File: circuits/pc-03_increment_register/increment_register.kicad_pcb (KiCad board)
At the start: 2 copper layers, 99.1 x 99.1 mm, 25 parts, among them J1 Conn_01x10, U1 74HC273, U10 4081, U11 4070, U12 4070, U13 4011, U2 74HC273, U3 74HC244, U4 74HC244, U5 74LS283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

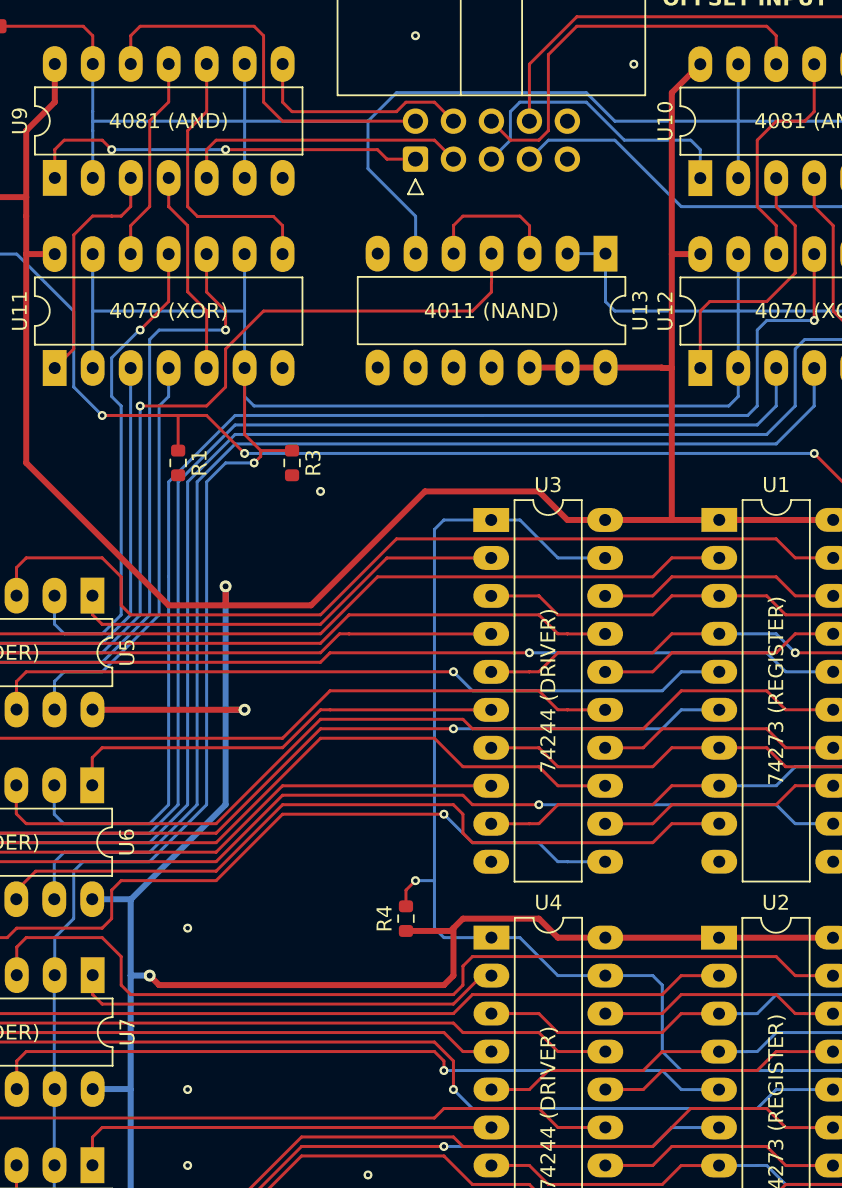
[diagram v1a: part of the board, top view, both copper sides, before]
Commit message: add filter and decoupling capacitors to all boards
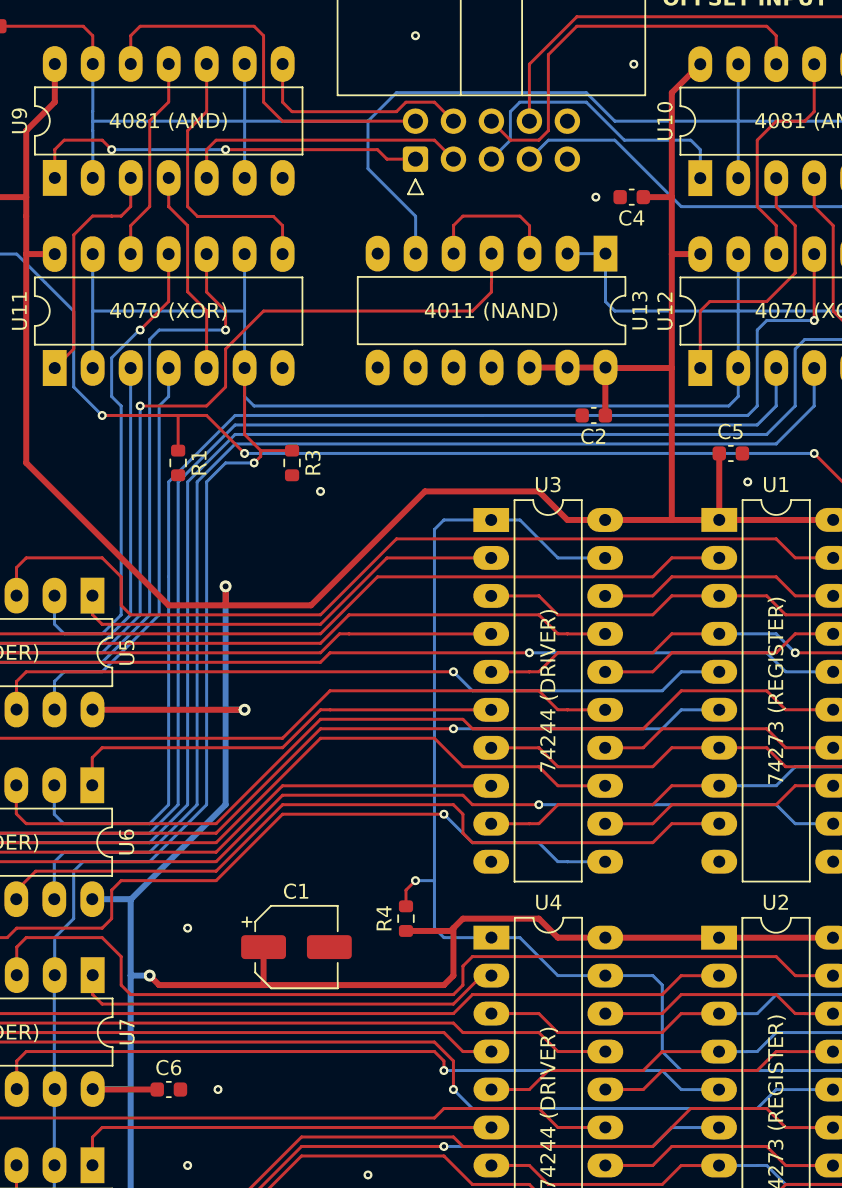
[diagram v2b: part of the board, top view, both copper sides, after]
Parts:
- added C1: C_Polarized, Capacitor_SMD:CP_Elec_5x5.3, F.Cu at (77.1, 89.5)
- added C2: C, Capacitor_SMD:C_0603_1608Metric, F.Cu at (97.0, 54.0)
- added C4: C, Capacitor_SMD:C_0603_1608Metric, F.Cu at (99.6, 39.4)
- added C5: C, Capacitor_SMD:C_0603_1608Metric, F.Cu at (106.2, 56.5)
- added C6: C, Capacitor_SMD:C_0603_1608Metric, F.Cu at (68.6, 99.1)
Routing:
- net VCC: track 263.6 -> 280.0 mm
- net GND: vias 12 -> 14

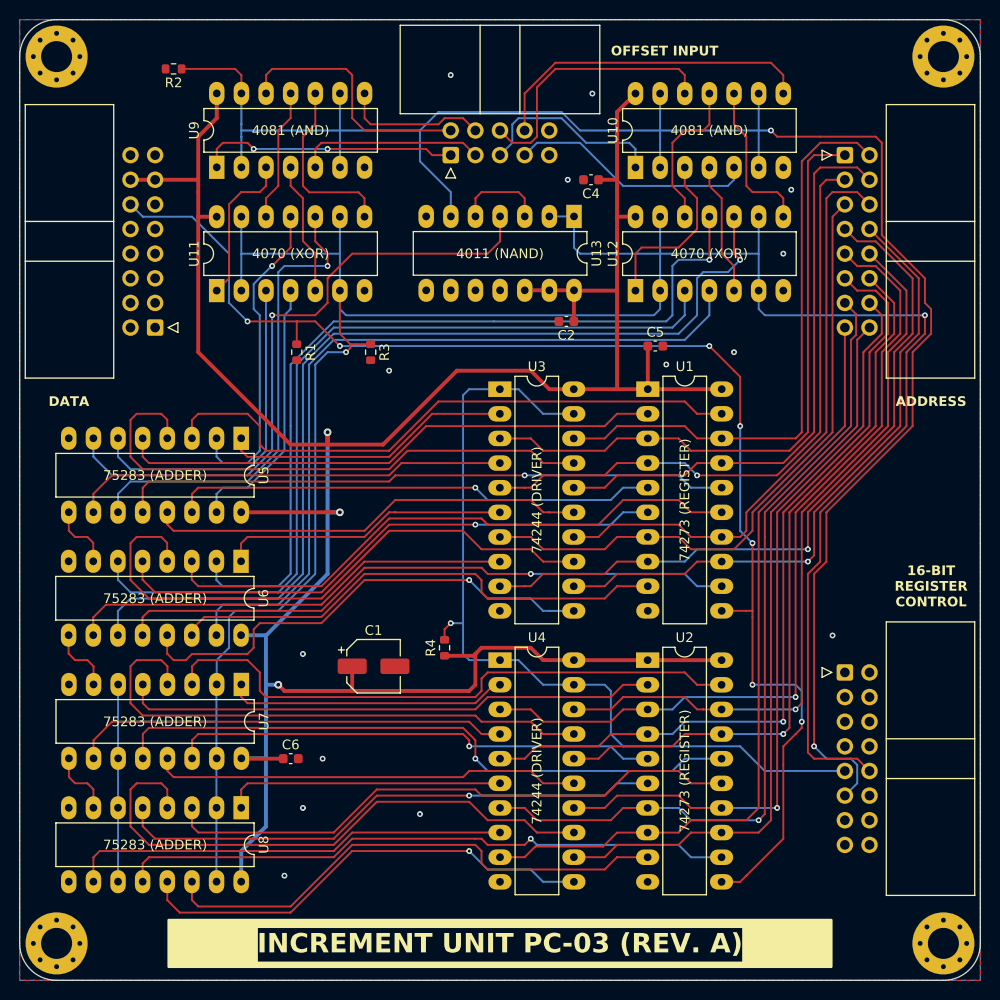
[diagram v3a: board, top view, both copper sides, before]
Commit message: PC-03: fix incrementer unit
 * adders are TTL, the weak pull-down on the `inc_dec` signal was not enough to drive the 8 directly connected adder pins correctly. Fixed through the introduction of a non-inverting buffer on that signal to produce hard signals in both directions.
 * incorrect logic caused decrement mode (INCR-1) to calculate (INCR-1+1) by mistake. reworked logic by replacing the old CD4011 NAND by a CD4070 XOR.
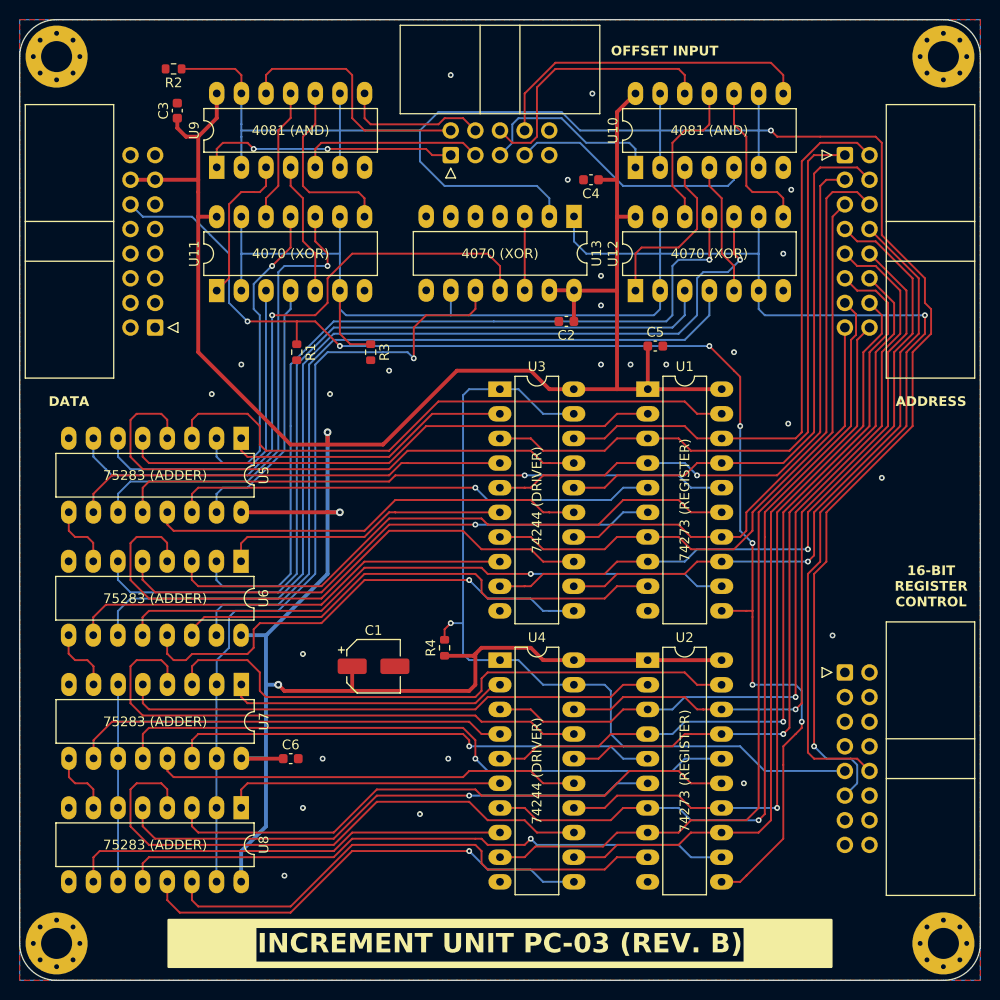
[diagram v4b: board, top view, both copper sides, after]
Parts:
- added C3: C, Capacitor_SMD:C_0603_1608Metric, F.Cu at (56.9, 32.2)
- U13: value 4011 -> 4070
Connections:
- U13 pad 10: unconnected-(U13-Pad10) -> /adder/inc_dec_driven
- U13 pad 11: unconnected-(U13-Pad11) -> /adder/carry_in
- U13 pad 12: VCC -> Net-(U13-Pad12)
- U13 pad 2: /inc_dec -> /inc_offset
- U13 pad 3: Net-(U13-Pad3) -> Net-(U13-Pad12)
- U13 pad 4: /adder/carry_in -> unconnected-(U13-Pad4)
- U13 pad 5: Net-(U13-Pad3) -> GND
- U13 pad 6: /inc_offset -> GND
- U13 pad 9: GND -> /inc_dec
- U7 pad 11: /inc_dec -> /adder/inc_dec_driven
- U7 pad 15: /inc_dec -> /adder/inc_dec_driven
- U7 pad 2: /inc_dec -> /adder/inc_dec_driven
- U7 pad 6: /inc_dec -> /adder/inc_dec_driven
- U8 pad 11: /inc_dec -> /adder/inc_dec_driven
- U8 pad 15: /inc_dec -> /adder/inc_dec_driven
- U8 pad 2: /inc_dec -> /adder/inc_dec_driven
- U8 pad 6: /inc_dec -> /adder/inc_dec_driven
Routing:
- net /adder/inc_dec_driven: track 0.00 -> 113.8 mm, vias 0 -> 1
- net /inc_dec: track 283.0 -> 187.3 mm, vias 2 -> 1
- net /inc_offset: track 195.4 -> 205.2 mm
- net Net-(U13-Pad3): track 9.36 -> 0.00 mm
- net Net-(U13-Pad12): track 0.00 -> 7.62 mm
- net VCC: track 280.0 -> 281.0 mm
- net GND: vias 14 -> 25
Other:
- board text added: "INCREMENT UNIT PC-03 (REV. B)"
- board text removed: "4011 (NAND)"
- board text removed: "INCREMENT UNIT PC-03 (REV. A)"

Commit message: pc-03: add double buffering to incrementer unit
This ensures stable data from the incrementer.
Previously, the published address would change at the start of the write cycle.
With the double buffering introduced, the current value of the address bus is latched into the first register at the start of the write cycle and pushed to the second register at the end of the write cycle.
This way the latched address is only seen by the incrementer at the start of the next cycle, ensuring a stable address bus state during the entire program step.
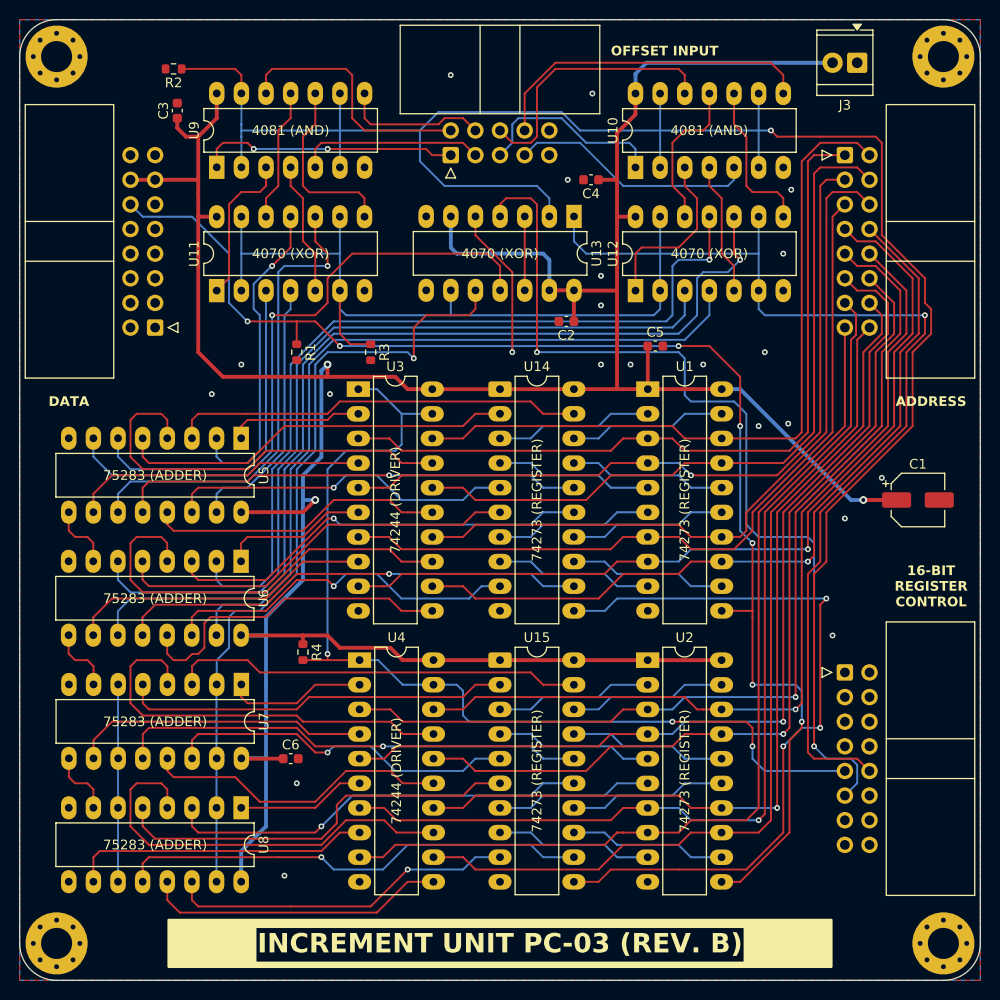
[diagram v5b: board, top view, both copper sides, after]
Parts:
- added J3: Screw_Terminal_01x02, TerminalBlock_TE-Connectivity:TerminalBlock_TE_282834-2_1x02_P2.54mm_Horizontal, F.Cu at (127.0, 27.3)
- added U14: 74HC273, Package_DIP:DIP-20_W7.62mm_LongPads, F.Cu at (90.2, 61.0)
- added U15: 74HC273, Package_DIP:DIP-20_W7.62mm_LongPads, F.Cu at (90.2, 88.9)
- moved C1 58.7 mm to (133.3, 72.4)
- moved R4 14.6 mm to (69.8, 88.1), turned to -90 degrees
- moved U3 14.6 mm to (75.6, 61.0)
- moved U4 14.5 mm to (75.7, 88.9)
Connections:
- net /adder/inc_dec_driven renamed /adder/dec_TTL
- net Net-(U13-Pad12) renamed /adder/~{carry_in}
- net Net-(U5-B1) renamed /adder/sec_0
- net Net-(U5-B2) renamed /adder/sec_1
- net Net-(U5-B3) renamed /adder/sec_2
- net Net-(U5-B4) renamed /adder/sec_3
- net Net-(U5-C4) renamed /adder/c4
- net Net-(U6-B1) renamed /adder/sec_4
- net Net-(U6-B2) renamed /adder/sec_5
- net Net-(U6-B3) renamed /adder/sec_6
- net Net-(U6-B4) renamed /adder/sec_7
- net Net-(U6-C4) renamed /adder/c8
- net Net-(U7-C4) renamed /adder/c12
- DATA_BUS1 pad 12: /clock -> clock
- R1 pad 1: /clock -> clock
- U1 pad 11: /clock -> clock
- U1 pad 12: /adder/reg7 -> /buf7
- U1 pad 15: /adder/reg5 -> /buf5
- U1 pad 16: /adder/reg3 -> /buf3
- U1 pad 19: /adder/reg1 -> /buf1
- U1 pad 2: /adder/reg0 -> /buf0
- U1 pad 5: /adder/reg2 -> /buf2
- U1 pad 6: /adder/reg4 -> /buf4
- U1 pad 9: /adder/reg6 -> /buf6
- U13 pad 4: unconnected-(U13-Pad4) -> ~{clock}
- U13 pad 5: GND -> clock
- U13 pad 6: GND -> VCC
- U2 pad 11: /clock -> clock
- U2 pad 12: /adder/reg15 -> /buf15
- U2 pad 15: /adder/reg13 -> /buf13
- U2 pad 16: /adder/reg11 -> /buf11
- U2 pad 19: /adder/reg9 -> /buf9
- U2 pad 2: /adder/reg8 -> /buf8
- U2 pad 5: /adder/reg10 -> /buf10
- U2 pad 6: /adder/reg12 -> /buf12
- U2 pad 9: /adder/reg14 -> /buf14
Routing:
- net clock: track 0.00 -> 156.8 mm, vias 0 -> 8
- net ~{clock}: track 0.00 -> 149.5 mm, vias 0 -> 4
- net /clock: track 140.6 -> 0.00 mm, vias 7 -> 0
- net VCC: track 281.0 -> 337.7 mm
- net /adder/reg1: track 62.1 -> 42.6 mm
- net /adder/reg9: track 61.8 -> 42.6 mm
- net /adder/reg14: track 54.1 -> 36.0 mm, vias 0 -> 1
- net /adder/reg11: track 65.9 -> 48.5 mm
- net /adder/reg5: track 61.6 -> 44.4 mm, vias 0 -> 1
- net /adder/inc14: track 48.3 -> 31.2 mm, vias 1 -> 0
- net /adder/reg13: track 60.5 -> 43.7 mm, vias 0 -> 1
- net /adder/inc4: track 60.7 -> 44.0 mm
- net /buf6: track 0.00 -> 16.3 mm
- net /buf4: track 0.00 -> 16.3 mm
- net /buf2: track 0.00 -> 16.3 mm
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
